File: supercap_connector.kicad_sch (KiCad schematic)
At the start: 0 parts

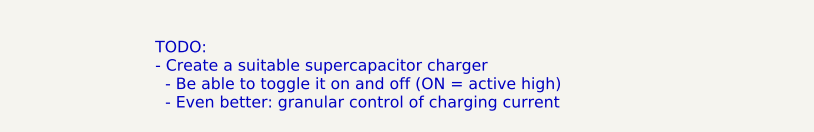
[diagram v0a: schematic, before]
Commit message: Added some text in the subsheets to outline what needs to be added inside of each subsheet
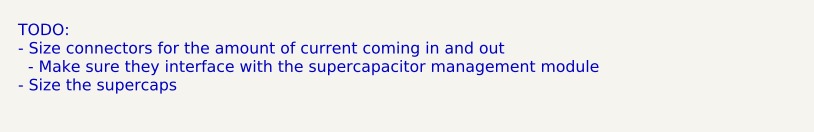
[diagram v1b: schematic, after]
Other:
- note added: "TODO: - Size connectors for the amount of current coming in and out - Make sure they interface with the supercapacitor management module - Size the supercaps"
- note removed: "TODO: - Create a suitable supercapacitor charger - Be able to toggle it on and off (ON = active high) - Even better: granular control of charging current"
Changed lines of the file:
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@@
 		(comment 1 "Robomaster")
 	)
-	(text "TODO:\n- Create a suitable supercapacitor charger\n  - Be able to toggle it on and off (ON = active high)\n  - Even better: granular control of charging current"
+	(text "TODO:\n- Size connectors for the amount of current coming in and out\n  - Make sure they interface with the supercapacitor management module\n- Size the supercaps"
 		(exclude_from_sim no)
-		(at 132.08 95.25 0)
+		(at 116.84 93.345 0)
 		(effects
 			(font
